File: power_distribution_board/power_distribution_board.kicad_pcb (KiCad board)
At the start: 2 copper layers, 67 parts, among them J1 CONN_01x03, J10 CONN_02X01, J11 CONN_02X01, J12 CONN_02X01, J13 CONN_02X01, J14 CONN_02X01, J15 CONN_02X01, J16 CONN_02X01, J17 CONN_02X01, J18 CONN_02X01, J19 CONN_02X01, J2 CONN_02X01, J20 CONN_02X01, J21 CONN_02X01, J22 CONN_02X01, J23 CONN_02X01, J3 CONN_02X01, J4 CONN_02X01, J5 CONN_02X01, J6 CONN_02X01, J7 CONN_02X01, J8 CONN_02X01, J9 CONN_02X01, Q1 NMOS_SSSGD, Q2 NMOS_SSSGD, Q3 NMOS_SSSGD, Q4 NMOS_SSSGD, Q5 Q_NMOS_GSD, U1 EHHD015A0A, U2 LTC1473, U3 EHHD010A0B, U4 LM317EMP, U5 BTS6133D, U6 A1120

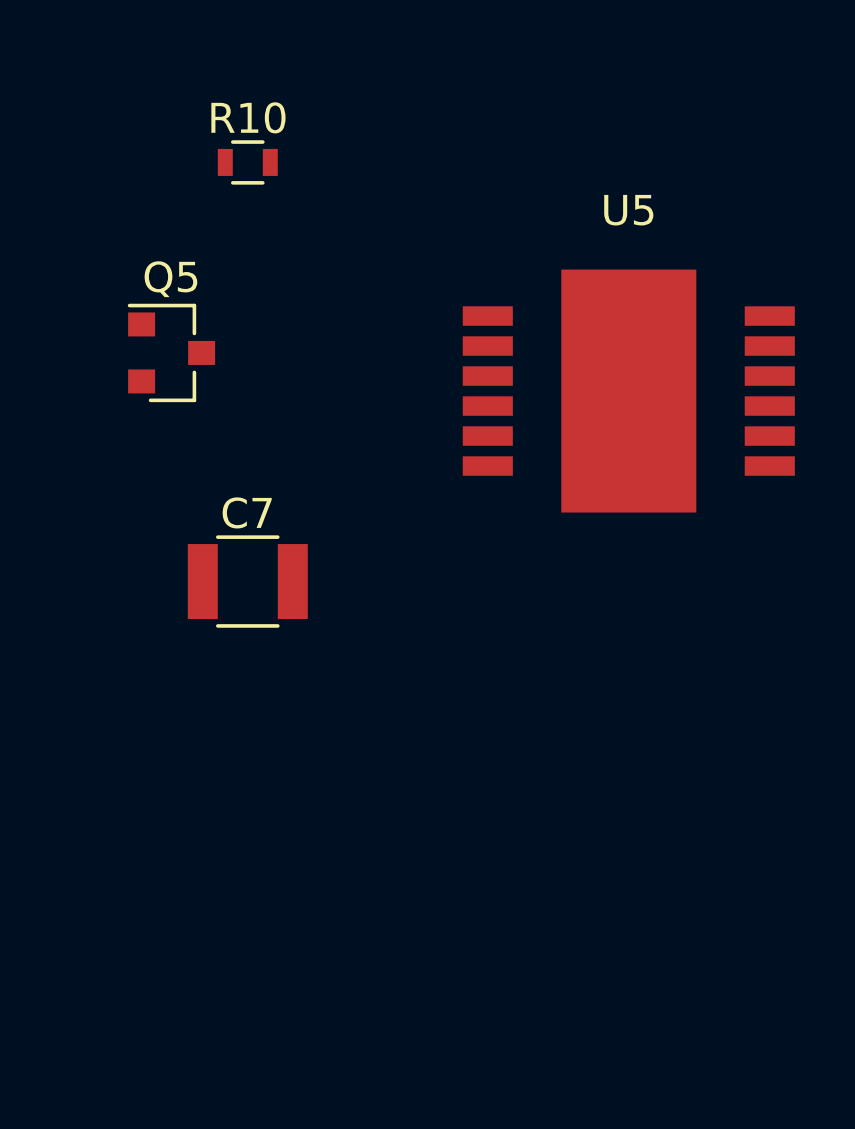
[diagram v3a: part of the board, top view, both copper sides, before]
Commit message: Update BTS6133D to have the correct footprint
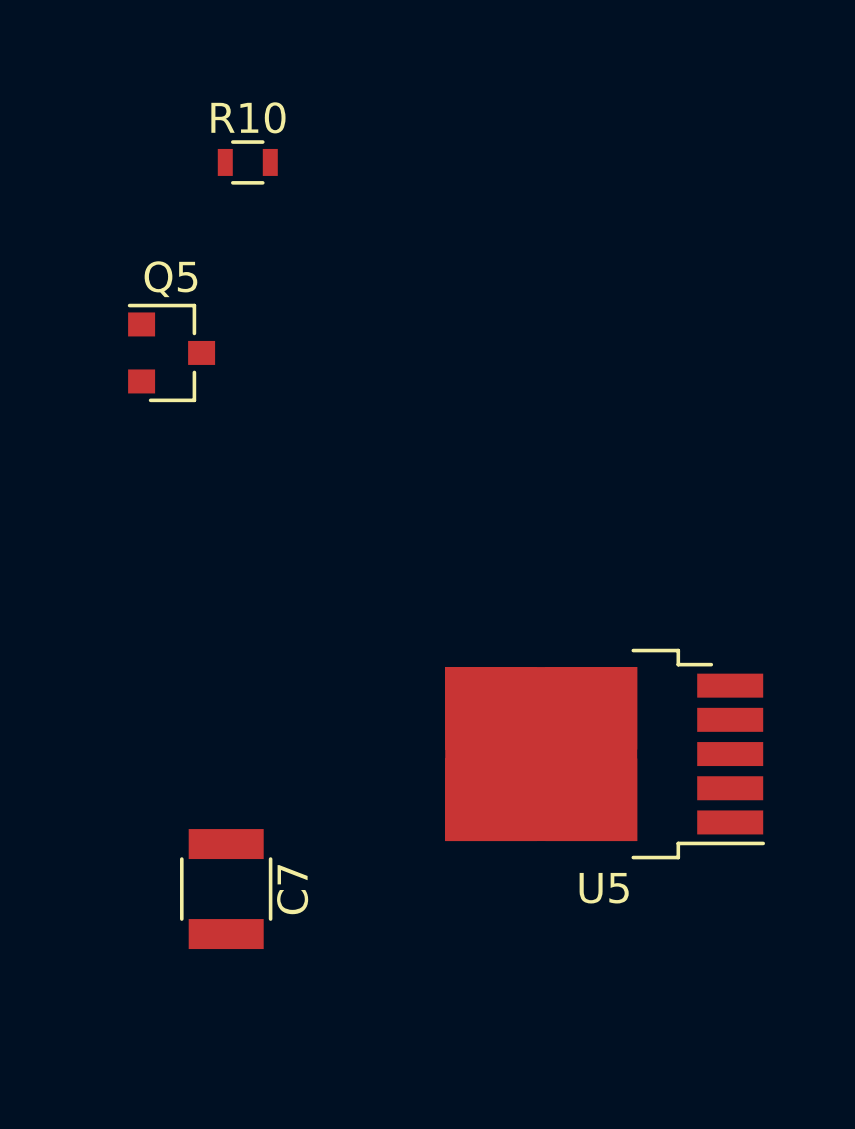
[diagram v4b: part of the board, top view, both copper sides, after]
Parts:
- U5: footprint cauv_lib:DSO-12-9 -> TO_SOT_Packages_SMD:TO-252-5_TabPin3
- moved U5 12.1 mm to (235.4, 113.7), turned to 180 degrees
- moved C7 10.3 mm to (222.8, 118.2), turned to 270 degrees
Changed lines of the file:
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@@
 (kicad_pcb (version 4) (host pcbnew 4.0.6)
   (general
-    (links 196)
-    (no_connects 119)
+    (links 201)
+    (no_connects 120)
     (area 0 0 0 0)
     (thickness 1.6)
@@
   )
   (module Capacitors_SMD:C_1210 (layer F.Cu)
-    (at 223.52 107.95)
+    (at 222.8 118.2 270)
     (descr "Capacitor SMD 1210, reflow soldering, AVX (see smccp.pdf)")
     (tags "capacitor 1210")
     (attr smd)
-    (fp_text reference C7 (at 0 -2.25) (layer F.SilkS)
+    (fp_text reference C7 (at 0 -2.25 270) (layer F.SilkS)
       (effects (font (size 1 1) (thickness 0.15)))
     )
-    (fp_text value 100μ (at 0 2.5) (layer F.Fab)
+    (fp_text value 100μ (at 0 2.5 270) (layer F.Fab)
       (effects (font (size 1 1) (thickness 0.15)))
     )
-    (fp_text user %R (at 0 -2.25) (layer F.Fab)
+    (fp_text user %R (at 0 -2.25 270) (layer F.Fab)
       (effects (font (size 1 1) (thickness 0.15)))
     )
@@
     (fp_line (start 2.25 1.5) (end 2.25 -1.5) (layer F.CrtYd) (width 0.05))
     (fp_line (start 2.25 1.5) (end -2.25 1.5) (layer F.CrtYd) (width 0.05))
-    (pad 1 smd rect (at -1.5 0) (size 1 2.5) (layers F.Cu F.Paste F.Mask)
+    (pad 1 smd rect (at -1.5 0 270) (size 1 2.5) (layers F.Cu F.Paste F.Mask)
       (net 5 /PWR_SWITCHED))
-    (pad 2 smd rect (at 1.5 0) (size 1 2.5) (layers F.Cu F.Paste F.Mask)
+    (pad 2 smd rect (at 1.5 0 270) (size 1 2.5) (layers F.Cu F.Paste F.Mask)
       (net 2 GND))
     (model Capacitors_SMD.3dshapes/C_1210.wrl
@@
     )
   )
-  (module cauv_lib:DSO-12-9 (layer F.Cu)
-    (at 236.22 101.6)
-    (fp_text reference U5 (at 0 -6 180) (layer F.SilkS)
-      (effects (font (size 1 1) (thickness 0.15)))
-    )
-    (fp_text value BTS6133D (at 0 5.5) (layer F.Fab)
-      (effects (font (size 1 1) (thickness 0.15)))
-    )
-    (fp_line (start 3.75 3.2) (end 3.75 -3.2) (layer F.Fab) (width 0.15))
-    (fp_line (start -3.75 -3.2) (end 3.75 -3.2) (layer F.Fab) (width 0.15))
-    (fp_line (start -3.75 3.2) (end -3.75 -3.2) (layer F.Fab) (width 0.15))
-    (fp_line (start -3.75 3.2) (end 3.75 3.2) (layer F.Fab) (width 0.15))
-    (fp_line (start -6 4.5) (end 6 4.5) (layer F.CrtYd) (width 0.01))
-    (fp_line (start 6 4.5) (end 6 -4.5) (layer F.CrtYd) (width 0.01))
-    (fp_line (start 6 -4.5) (end -6 -4.5) (layer F.CrtYd) (width 0.01))
-    (fp_line (start -6 -4.5) (end -6 4.5) (layer F.CrtYd) (width 0.01))
-    (pad 12 smd rect (at -4.7 2.5 90) (size 0.65 1.67) (layers F.Cu F.Paste F.Mask))
-    (pad 1 smd rect (at 4.7 2.5 90) (size 0.65 1.67) (layers F.Cu F.Paste F.Mask)
-      (net 17 /20V_PWR))
-    (pad 11 smd rect (at -4.7 1.5 90) (size 0.65 1.67) (layers F.Cu F.Paste F.Mask))
-    (pad 2 smd rect (at 4.7 1.5 90) (size 0.65 1.67) (layers F.Cu F.Paste F.Mask)
-      (net 28 "Net-(Q5-Pad3)"))
-    (pad 10 smd rect (at -4.7 0.5 90) (size 0.65 1.67) (layers F.Cu F.Paste F.Mask))
-    (pad 3 smd rect (at 4.7 0.5 90) (size 0.65 1.67) (layers F.Cu F.Paste F.Mask)
-      (net 5 /PWR_SWITCHED))
-    (pad 9 smd rect (at -4.7 -0.5 90) (size 0.65 1.67) (layers F.Cu F.Paste F.Mask))
-    (pad 4 smd rect (at 4.7 -0.5 90) (size 0.65 1.67) (layers F.Cu F.Paste F.Mask)
-      (net 37 "Net-(U5-Pad4)"))
-    (pad 8 smd rect (at -4.7 -1.5 90) (size 0.65 1.67) (layers F.Cu F.Paste F.Mask))
-    (pad 5 smd rect (at 4.7 -1.5 90) (size 0.65 1.67) (layers F.Cu F.Paste F.Mask)
-      (net 17 /20V_PWR))
-    (pad 7 smd rect (at -4.7 -2.5 90) (size 0.65 1.67) (layers F.Cu F.Paste F.Mask))
-    (pad 6 smd rect (at 4.7 -2.5 90) (size 0.65 1.67) (layers F.Cu F.Paste F.Mask))
-    (pad 13 smd rect (at 0 0 90) (size 8.1 4.5) (layers F.Cu F.Paste F.Mask))
-  )
   (module Connectors_Molex:Molex_KK-6410-03_03x2.54mm_Straight (layer F.Cu)
     (at 166.6 130.2 270)
@@
       (at (xyz 0 0 0))
       (scale (xyz 1 1 1))
+      (rotate (xyz 0 0 0))
+    )
+  )
+  (module TO_SOT_Packages_SMD:TO-252-5_TabPin3 (layer F.Cu)
+    (at 235.4 113.7 180)
+    (descr "TO-252 / DPAK SMD package, http://www.infineon.com/cms/en/product/packages/PG-TO252/PG-TO252-5-11/")
+    (tags "DPAK TO-252 DPAK-5 TO-252-5")
+    (attr smd)
+    (fp_text reference U5 (at 0 -4.5 180) (layer F.SilkS)
+      (effects (font (size 1 1) (thickness 0.15)))
+    )
+    (fp_text value BTS6133D (at 0 4.5 180) (layer F.Fab)
+      (effects (font (size 1 1) (thickness 0.15)))
+    )
+    (fp_line (start 3.95 -2.7) (end 4.95 -2.7) (layer F.Fab) (width 0.1))
+    (fp_line (start 4.95 -2.7) (end 4.95 2.7) (layer F.Fab) (width 0.1))
+    (fp_line (start 4.95 2.7) (end 3.95 2.7) (layer F.Fab) (width 0.1))
+    (fp_line (start 3.95 -3.25) (end 3.95 3.25) (layer F.Fab) (width 0.1))
+    (fp_line (start 3.95 3.25) (end -2.27 3.25) (layer F.Fab) (width 0.1))
+    (fp_line (start -2.27 3.25) (end -2.27 -2.25) (layer F.Fab) (width 0.1))
+    (fp_line (start -2.27 -2.25) (end -1.27 -3.25) (layer F.Fab) (width 0.1))
+    (fp_line (start -1.27 -3.25) (end 3.95 -3.25) (layer F.Fab) (width 0.1))
+    (fp_line (start -1.94 -2.58) (end -4.97 -2.58) (layer F.Fab) (width 0.1))
+    (fp_line (start -4.97 -2.58) (end -4.97 -1.98) (layer F.Fab) (width 0.1))
+    (fp_line (start -4.97 -1.98) (end -2.27 -1.98) (layer F.Fab) (width 0.1))
+    (fp_line (start -2.27 -1.44) (end -4.97 -1.44) (layer F.Fab) (width 0.1))
+    (fp_line (start -4.97 -1.44) (end -4.97 -0.84) (layer F.Fab) (width 0.1))
+    (fp_line (start -4.97 -0.84) (end -2.27 -0.84) (layer F.Fab) (width 0.1))
+    (fp_line (start -2.27 -0.3) (end -4.97 -0.3) (layer F.Fab) (width 0.1))
+    (fp_line (start -4.97 -0.3) (end -4.97 0.3) (layer F.Fab) (width 0.1))
+    (fp_line (start -4.97 0.3) (end -2.27 0.3) (layer F.Fab) (width 0.1))
+    (fp_line (start -2.27 0.84) (end -4.97 0.84) (layer F.Fab) (width 0.1))
+    (fp_line (start -4.97 0.84) (end -4.97 1.44) (layer F.Fab) (width 0.1))
+    (fp_line (start -4.97 1.44) (end -2.27 1.44) (layer F.Fab) (width 0.1))
+    (fp_line (start -2.27 1.98) (end -4.97 1.98) (layer F.Fab) (width 0.1))
+    (fp_line (start -4.97 1.98) (end -4.97 2.58) (layer F.Fab) (width 0.1))
+    (fp_line (start -4.97 2.58) (end -2.27 2.58) (layer F.Fab) (width 0.1))
+    (fp_line (start -0.97 -3.45) (end -2.47 -3.45) (layer F.SilkS) (width 0.12))
+    (fp_line (start -2.47 -3.45) (end -2.47 -2.98) (layer F.SilkS) (width 0.12))
+    (fp_line (start -2.47 -2.98) (end -5.3 -2.98) (layer F.SilkS) (width 0.12))
+    (fp_line (start -0.97 3.45) (end -2.47 3.45) (layer F.SilkS) (width 0.12))
+    (fp_line (start -2.47 3.45) (end -2.47 2.98) (layer F.SilkS) (width 0.12))
+    (fp_line (start -2.47 2.98) (end -3.57 2.98) (layer F.SilkS) (width 0.12))
+    (fp_line (start -5.55 -3.5) (end -5.55 3.5) (layer F.CrtYd) (width 0.05))
+    (fp_line (start -5.55 3.5) (end 5.55 3.5) (layer F.CrtYd) (width 0.05))
+    (fp_line (start 5.55 3.5) (end 5.55 -3.5) (layer F.CrtYd) (width 0.05))
+    (fp_line (start 5.55 -3.5) (end -5.55 -3.5) (layer F.CrtYd) (width 0.05))
+    (fp_text user %R (at 0 0 180) (layer F.Fab)
+      (effects (font (size 1 1) (thickness 0.15)))
+    )
+    (pad 1 smd rect (at -4.2 -2.28 180) (size 2.2 0.8) (layers F.Cu F.Paste F.Mask)
+      (net 17 /20V_PWR))
+    (pad 2 smd rect (at -4.2 -1.14 180) (size 2.2 0.8) (layers F.Cu F.Paste F.Mask)
+      (net 28 "Net-(Q5-Pad3)"))
+    (pad 3 smd rect (at -4.2 0 180) (size 2.2 0.8) (layers F.Cu F.Paste F.Mask)
+      (net 5 /PWR_SWITCHED))
+    (pad 4 smd rect (at -4.2 1.14 180) (size 2.2 0.8) (layers F.Cu F.Paste F.Mask)
+      (net 37 "Net-(U5-Pad4)"))
+    (pad 5 smd rect (at -4.2 2.28 180) (size 2.2 0.8) (layers F.Cu F.Paste F.Mask)
+      (net 17 /20V_PWR))
+    (pad 3 smd rect (at 2.1 0 180) (size 6.4 5.8) (layers F.Cu F.Mask)
+      (net 5 /PWR_SWITCHED))
+    (pad 3 smd rect (at 3.775 1.525 180) (size 3.05 2.75) (layers F.Cu F.Paste)
+      (net 5 /PWR_SWITCHED))
+    (pad 3 smd rect (at 0.425 -1.525 180) (size 3.05 2.75) (layers F.Cu F.Paste)
+      (net 5 /PWR_SWITCHED))
+    (pad 3 smd rect (at 3.775 -1.525 180) (size 3.05 2.75) (layers F.Cu F.Paste)
+      (net 5 /PWR_SWITCHED))
+    (pad 3 smd rect (at 0.425 1.525 180) (size 3.05 2.75) (layers F.Cu F.Paste)
+      (net 5 /PWR_SWITCHED))
+    (model ${KISYS3DMOD}/TO_SOT_Packages_SMD.3dshapes/TO-252-5_TabPin3.wrl
+      (at (xyz 0 0 0))
+      (scale (xyz 1 1 1))

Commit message: improvements to layout of killswitch subcircuit
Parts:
- moved D1 216.9 mm to (13.1, -42.3)
- moved R1 216.9 mm to (18.2, -42.3)
- moved TP1 216.9 mm to (23.2, -42.3)
- moved D2 184.3 mm to (17.2, 35.0)
- moved R2 184.3 mm to (22.3, 35.0)
- moved TP2 184.3 mm to (27.3, 35.0)
- moved TP4 78.5 mm to (156.7, 128.6)
- moved D7 78.1 mm to (156.7, 135.1), turned to 90 degrees
- moved R4 77.6 mm to (156.7, 131.3), turned to 270 degrees
- moved R3 45.4 mm to (243.9, 100.3)
- moved D4 45.4 mm to (238.8, 100.3)
- moved TP3 45.4 mm to (248.9, 100.3)
- moved R13 11.4 mm to (160.3, 131.3)
- moved Q5 7.70 mm to (215.1, 105.3)
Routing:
- net /PWR_ENABLE: track 5.39 -> 12.8 mm
- net Net-(D7-Pad2): track 0.00 -> 1.95 mm
- net /AO_PWR: track 20.5 -> 21.7 mm
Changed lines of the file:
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@@
   (general
     (links 201)
-    (no_connects 120)
+    (no_connects 117)
     (area 0 0 0 0)
     (thickness 1.6)
     (drawings 0)
-    (tracks 97)
+    (tracks 101)
     (zones 0)
     (modules 67)
@@
   )
   (module LEDs:LED_0805 (layer F.Cu)
-    (at 195.58 74.93)
+    (at 13.08 -42.27)
     (descr "LED 0805 smd package")
     (tags "LED led 0805 SMD smd SMT smt smdled SMDLED smtled SMTLED")
@@
   )
   (module LEDs:LED_0805 (layer F.Cu)
-    (at 195.58 81.28)
+    (at 17.18 34.98)
     (descr "LED 0805 smd package")
     (tags "LED led 0805 SMD smd SMT smt smdled SMDLED smtled SMTLED")
@@
   )
   (module LEDs:LED_0805 (layer F.Cu)
-    (at 195.58 86.36)
+    (at 238.78 100.26)
     (descr "LED 0805 smd package")
     (tags "LED led 0805 SMD smd SMT smt smdled SMDLED smtled SMTLED")
@@
   )
   (module LEDs:LED_0805 (layer F.Cu)
-    (at 195.58 67.31)
+    (at 156.7 135.1 90)
     (descr "LED 0805 smd package")
     (tags "LED led 0805 SMD smd SMT smt smdled SMDLED smtled SMTLED")
     (attr smd)
-    (fp_text reference D7 (at 0 -1.45) (layer F.SilkS)
+    (fp_text reference D7 (at 0 -1.45 90) (layer F.SilkS)
       (effects (font (size 1 1) (thickness 0.15)))
     )
-    (fp_text value LED (at 0 1.55) (layer F.Fab)
+    (fp_text value LED (at 0 1.55 90) (layer F.Fab)
       (effects (font (size 1 1) (thickness 0.15)))
     )
@@
     (fp_line (start -1.95 0.85) (end -1.95 -0.85) (layer F.CrtYd) (width 0.05))
     (fp_line (start -1.95 -0.85) (end 1.95 -0.85) (layer F.CrtYd) (width 0.05))
-    (pad 2 smd rect (at 1.1 0 180) (size 1.2 1.2) (layers F.Cu F.Paste F.Mask)
+    (pad 2 smd rect (at 1.1 0 270) (size 1.2 1.2) (layers F.Cu F.Paste F.Mask)
       (net 12 "Net-(D7-Pad2)"))
-    (pad 1 smd rect (at -1.1 0 180) (size 1.2 1.2) (layers F.Cu F.Paste F.Mask)
+    (pad 1 smd rect (at -1.1 0 270) (size 1.2 1.2) (layers F.Cu F.Paste F.Mask)
       (net 2 GND))
     (model ${KISYS3DMOD}/LEDs.3dshapes/LED_0805.wrl
@@
   )
   (module TO_SOT_Packages_SMD:SOT-23 (layer F.Cu)
-    (at 220.98 100.33)
+    (at 215.1 105.3)
     (descr "SOT-23, Standard")
     (tags SOT-23)
@@
   )
   (module Resistors_SMD:R_0603 (layer F.Cu)
-    (at 200.66 74.93)
+    (at 18.16 -42.27)
     (descr "Resistor SMD 0603, reflow soldering, Vishay (see dcrcw.pdf)")
     (tags "resistor 0603")
@@
   )
   (module Resistors_SMD:R_0603 (layer F.Cu)
-    (at 200.66 81.28)
+    (at 22.26 34.98)
     (descr "Resistor SMD 0603, reflow soldering, Vishay (see dcrcw.pdf)")
     (tags "resistor 0603")
@@
   )
   (module Resistors_SMD:R_0603 (layer F.Cu)
-    (at 200.66 86.36)
+    (at 243.86 100.26)
     (descr "Resistor SMD 0603, reflow soldering, Vishay (see dcrcw.pdf)")
     (tags "resistor 0603")
@@
   )
   (module Resistors_SMD:R_0603 (layer F.Cu)
-    (at 200.66 67.31)
+    (at 156.7 131.3 270)
     (descr "Resistor SMD 0603, reflow soldering, Vishay (see dcrcw.pdf)")
     (tags "resistor 0603")
     (attr smd)
-    (fp_text reference R4 (at 0 -1.45) (layer F.SilkS)
+    (fp_text reference R4 (at 0 3.2 270) (layer F.SilkS)
       (effects (font (size 1 1) (thickness 0.15)))
     )
-    (fp_text value 1.5k (at 0 1.5) (layer F.Fab)
+    (fp_text value 1.5k (at 0 5 270) (layer F.Fab)
       (effects (font (size 1 1) (thickness 0.15)))
     )
-    (fp_text user %R (at 0 0) (layer F.Fab)
+    (fp_text user %R (at 0 0 270) (layer F.Fab)
       (effects (font (size 0.4 0.4) (thickness 0.075)))
     )
@@
     (fp_line (start 1.25 0.7) (end 1.25 -0.7) (layer F.CrtYd) (width 0.05))
     (fp_line (start 1.25 0.7) (end -1.25 0.7) (layer F.CrtYd) (width 0.05))
-    (pad 1 smd rect (at -0.75 0) (size 0.5 0.9) (layers F.Cu F.Paste F.Mask)
+    (pad 1 smd rect (at -0.75 0 270) (size 0.5 0.9) (layers F.Cu F.Paste F.Mask)
       (net 27 /PWR_ENABLE))
-    (pad 2 smd rect (at 0.75 0) (size 0.5 0.9) (layers F.Cu F.Paste F.Mask)
+    (pad 2 smd rect (at 0.75 0 270) (size 0.5 0.9) (layers F.Cu F.Paste F.Mask)
       (net 12 "Net-(D7-Pad2)"))
     (model ${KISYS3DMOD}/Resistors_SMD.3dshapes/R_0603.wrl
@@
   )
   (module Resistors_SMD:R_0603 (layer F.Cu)
-    (at 171.7 131.3 90)
+    (at 160.3 131.3 90)
     (descr "Resistor SMD 0603, reflow soldering, Vishay (see dcrcw.pdf)")
     (tags "resistor 0603")
@@
   )
   (module agg_lib:TESTPAD (layer F.Cu)
-    (at 205.74 74.93)
+    (at 23.24 -42.27)
     (fp_text reference TP1 (at 0 -1.4) (layer F.Fab) hide
       (effects (font (size 1 1) (thickness 0.15)))
@@
   )
   (module agg_lib:TESTPAD (layer F.Cu)
-    (at 205.74 81.28)
+    (at 27.34 34.98)
     (fp_text reference TP2 (at 0 -1.4) (layer F.Fab) hide
       (effects (font (size 1 1) (thickness 0.15)))
@@
   )
   (module agg_lib:TESTPAD (layer F.Cu)
-    (at 205.74 86.36)
+    (at 248.94 100.26)
     (fp_text reference TP3 (at 0 -1.4) (layer F.Fab) hide
       (effects (font (size 1 1) (thickness 0.15)))
@@
   )
   (module agg_lib:TESTPAD (layer F.Cu)
-    (at 205.74 67.31)
+    (at 156.7 128.6)
     (fp_text reference TP4 (at 0 -1.4) (layer F.Fab) hide
       (effects (font (size 1 1) (thickness 0.15)))
@@
   (segment (start 160.8 124.45) (end 160.95 124.3) (width 0.2) (layer F.Cu) (net 5))
   (segment (start 160.95 124.3) (end 163.45 124.3) (width 0.2) (layer F.Cu) (net 5))
-  (segment (start 171.7 130.55) (end 171.35 130.2) (width 0.4) (layer F.Cu) (net 6))
-  (segment (start 171.35 130.2) (end 166.6 130.2) (width 0.4) (layer F.Cu) (net 6))
+  (segment (start 166.6 130.2) (end 166.25 130.55) (width 0.4) (layer F.Cu) (net 6) (status C00000))
+  (segment (start 166.25 130.55) (end 160.3 130.55) (width 0.4) (layer F.Cu) (net 6) (status C00000))
   (segment (start 165.15 127.1) (end 166.6 127.1) (width 0.4) (layer F.Cu) (net 6))
   (segment (start 166.6 127.1) (end 166.6 127) (width 0.4) (layer F.Cu) (net 6))
@@
   (segment (start 163.45 122) (end 163 121.55) (width 0.2) (layer F.Cu) (net 6))
   (segment (start 163 121.55) (end 160.6 121.55) (width 0.2) (layer F.Cu) (net 6) (status 20))
+  (segment (start 156.7 134) (end 156.7 132.05) (width 0.2) (layer F.Cu) (net 12) (status C00000))
   (segment (start 57 132.25) (end 57.25 132.25) (width 0.2) (layer F.Cu) (net 13))
   (segment (start 57.25 132.25) (end 57.75 131.75) (width 0.2) (layer F.Cu) (net 13))
@@
   (segment (start 64.75 140.75) (end 62.3875 140.75) (width 0.2) (layer F.Cu) (net 26))
   (segment (start 62.3875 140.75) (end 62.29 140.6525) (width 0.2) (layer F.Cu) (net 26))
-  (segment (start 171.7 132.05) (end 171.01 132.74) (width 0.2) (layer F.Cu) (net 27))
-  (segment (start 171.01 132.74) (end 166.6 132.74) (width 0.2) (layer F.Cu) (net 27))
+  (segment (start 156.7 130.55) (end 156.7 128.6) (width 0.2) (layer F.Cu) (net 27) (status C00000))
+  (segment (start 156.7 130.55) (end 158.2 132.05) (width 0.2) (layer F.Cu) (net 27) (status 400000))
+  (segment (start 158.2 132.05) (end 160.3 132.05) (width 0.2) (layer F.Cu) (net 27) (status 800000))
+  (segment (start 166.6 132.74) (end 165.91 132.05) (width 0.2) (layer F.Cu) (net 27) (status C00000))
+  (segment (start 165.91 132.05) (end 160.3 132.05) (width 0.2) (layer F.Cu) (net 27) (status C00000))
   (segment (start 55.25 137.4775) (end 54.7725 137) (width 0.2) (layer F.Cu) (net 29))
   (segment (start 54.7725 137) (end 53 137) (width 0.2) (layer F.Cu) (net 29))
